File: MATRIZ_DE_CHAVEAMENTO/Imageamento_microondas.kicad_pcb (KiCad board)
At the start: 4 copper layers, 200 x 150 mm, 121 parts, among them J1 0732511352, J10 0732511352, J11 TB0012-508-03GR, J12 0732511352, J13 0732511352, J2 0732511352, J3 0732511352, J4 0732511352, J5 0732511352, J6 0732511352, J7 0732511352, J8 0732511352, J9 0732511352, U1 SKY13373-460LF, U10 SKY13373-460LF, U11 SKY13373-460LF, U12 SKY13373-460LF, U13 SKY13373-460LF, U14 SKY13373-460LF, U15 SKY13373-460LF, U16 SKY13373-460LF, U17 ESP32-DEVKITC-32E, U18 MCP23016-I_SP, U2 SKY13373-460LF, U3 SKY13373-460LF, U4 SKY13373-460LF, U5 SKY13373-460LF, U6 SKY13373-460LF, U7 SKY13373-460LF, U8 SKY13373-460LF, U9 SKY13373-460LF

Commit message: ci(files): project files added
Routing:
- net GND: vias 2194 -> 2258
- net /CA_5: vias 1 -> 2

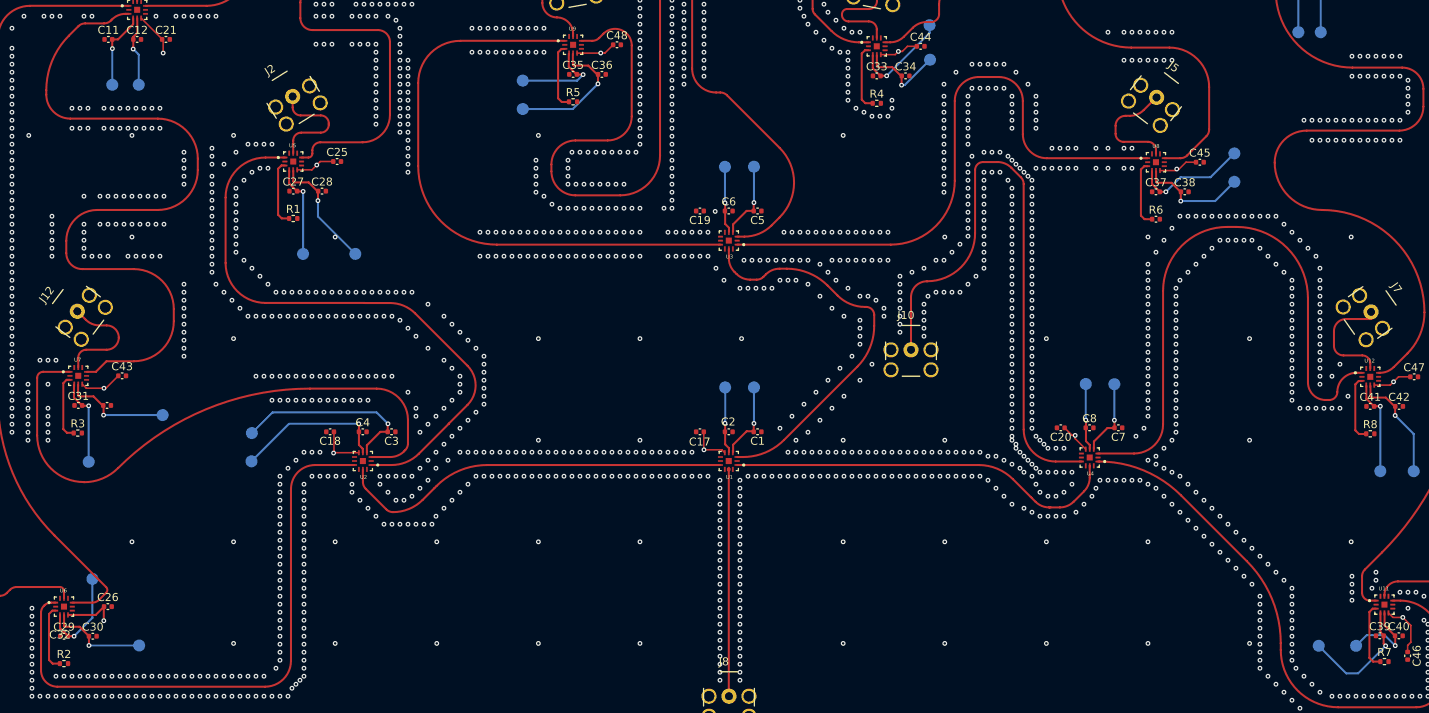
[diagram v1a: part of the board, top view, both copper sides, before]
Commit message: feat(footprint): RF switch footprint updated
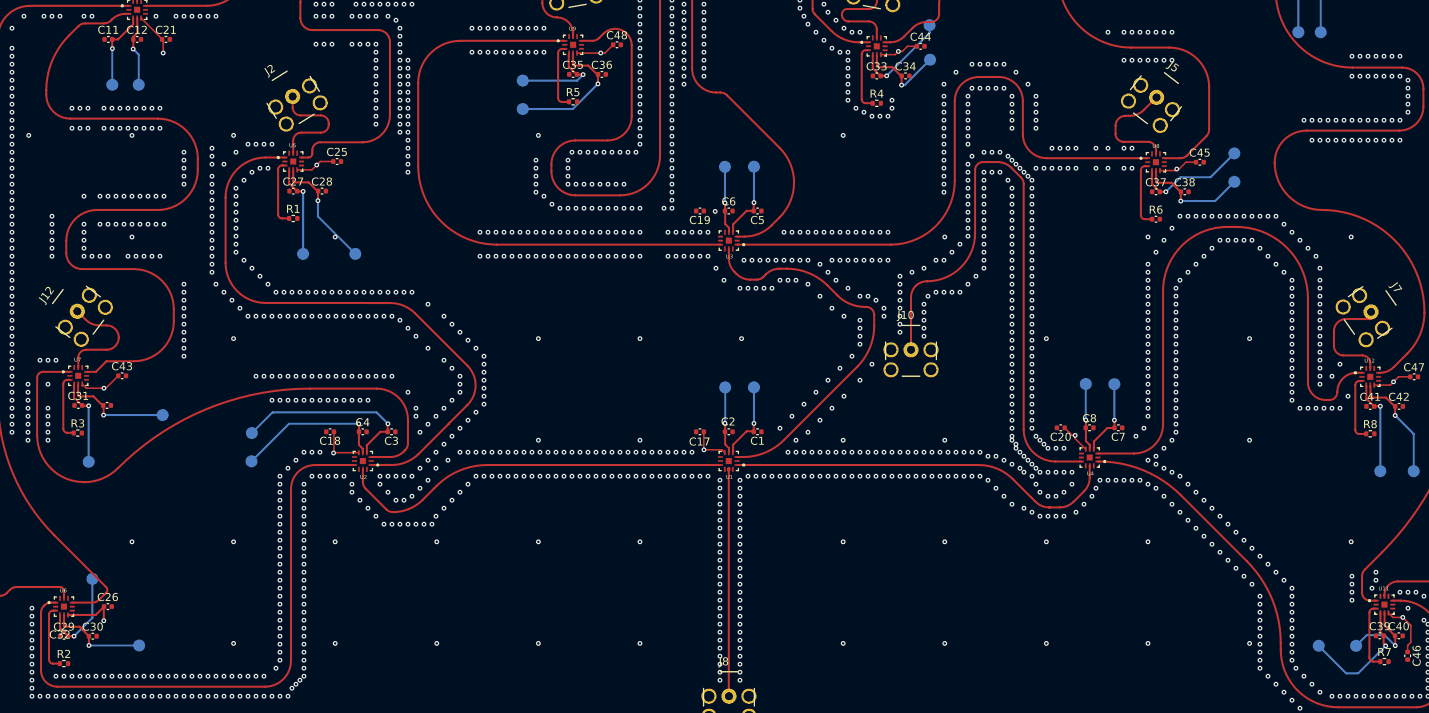
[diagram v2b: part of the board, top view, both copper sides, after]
